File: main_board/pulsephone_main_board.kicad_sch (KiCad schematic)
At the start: 22 parts, among them J3 Conn_2Rows-35Pins_MountingPin, J4 Conn_2Rows-35Pins_MountingPin, J5 Conn_2Rows-35Pins_MountingPin, U1 XL1509-3.3, U2 PCM5102APWR, U4 TPS61202DRC

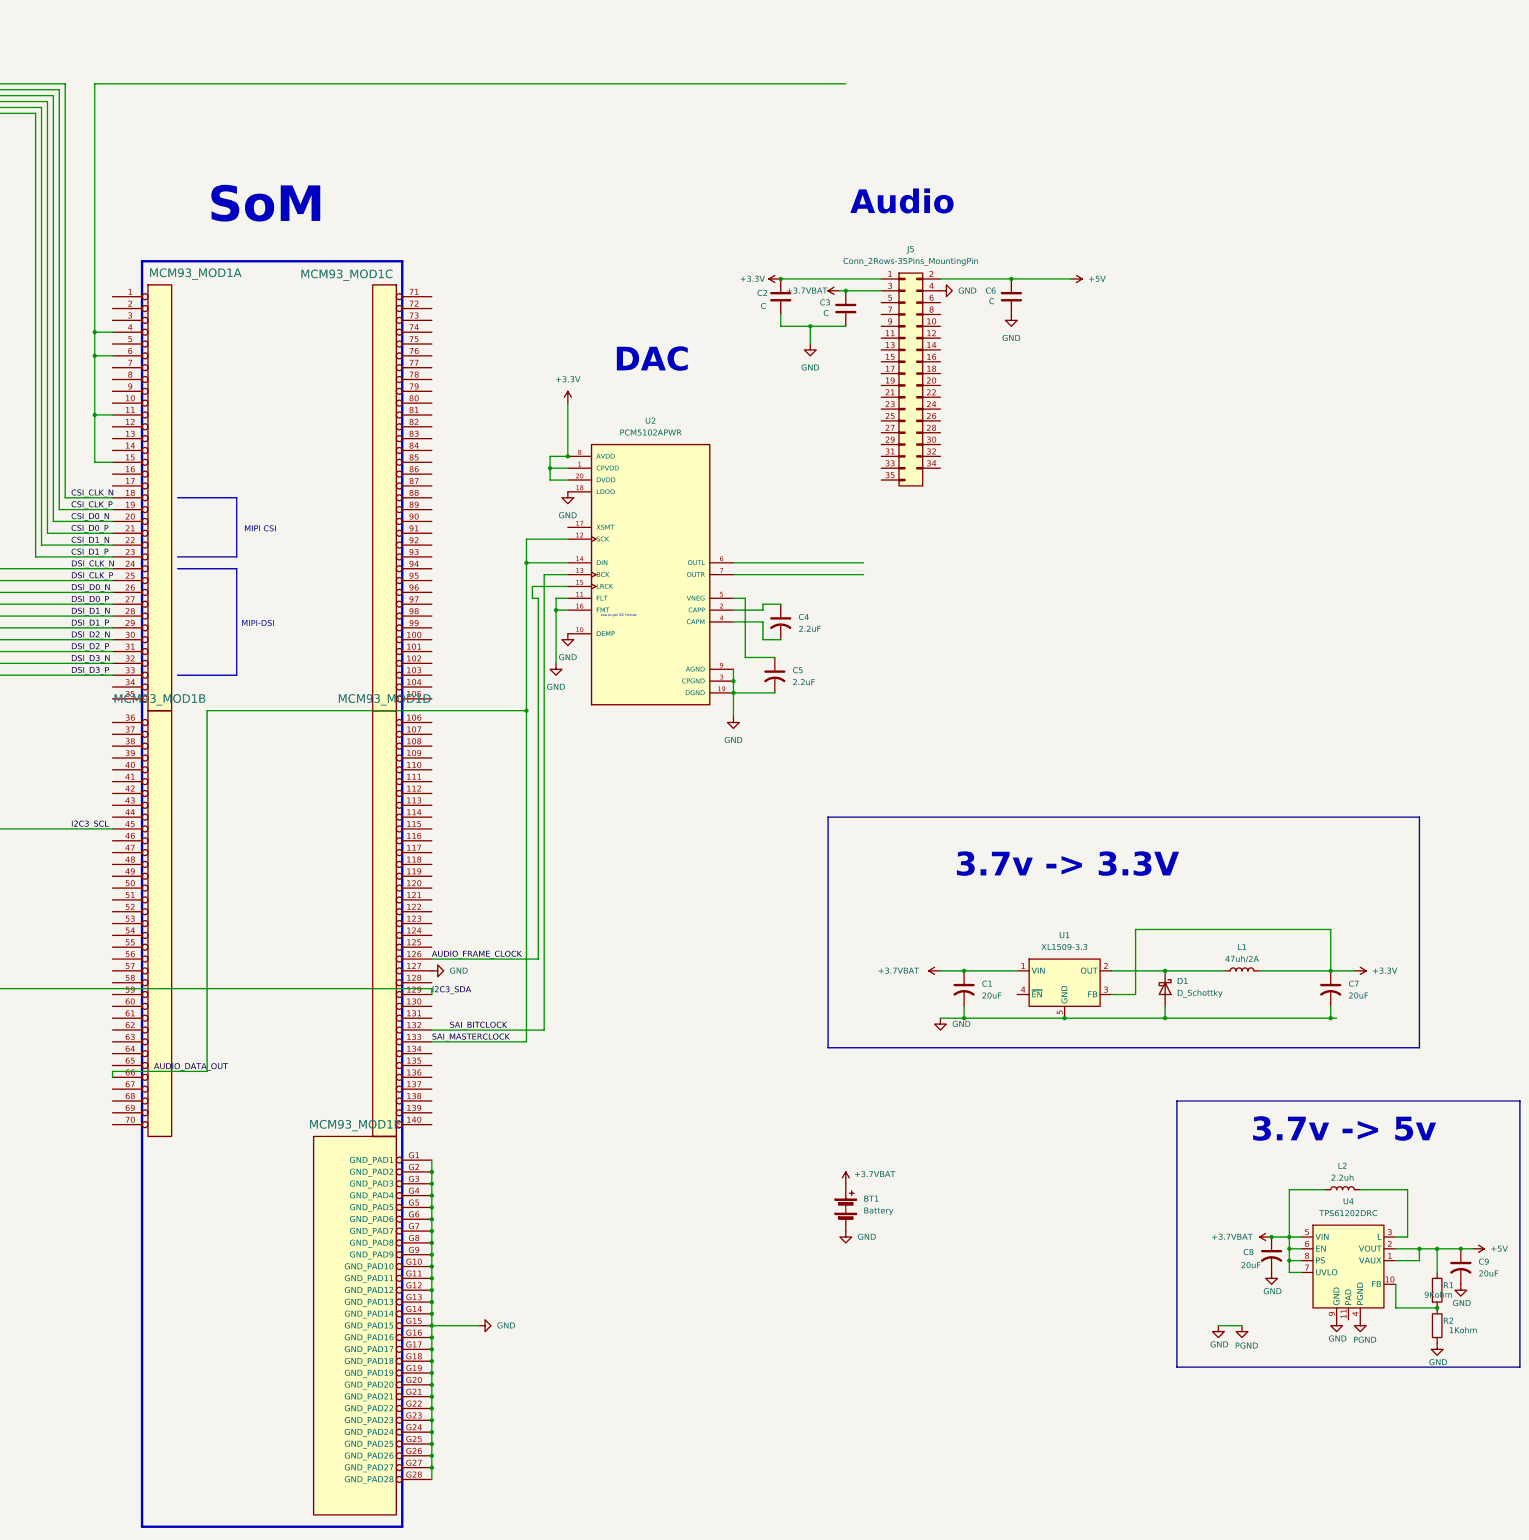
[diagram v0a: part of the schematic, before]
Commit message: Add in new, researched PMICs
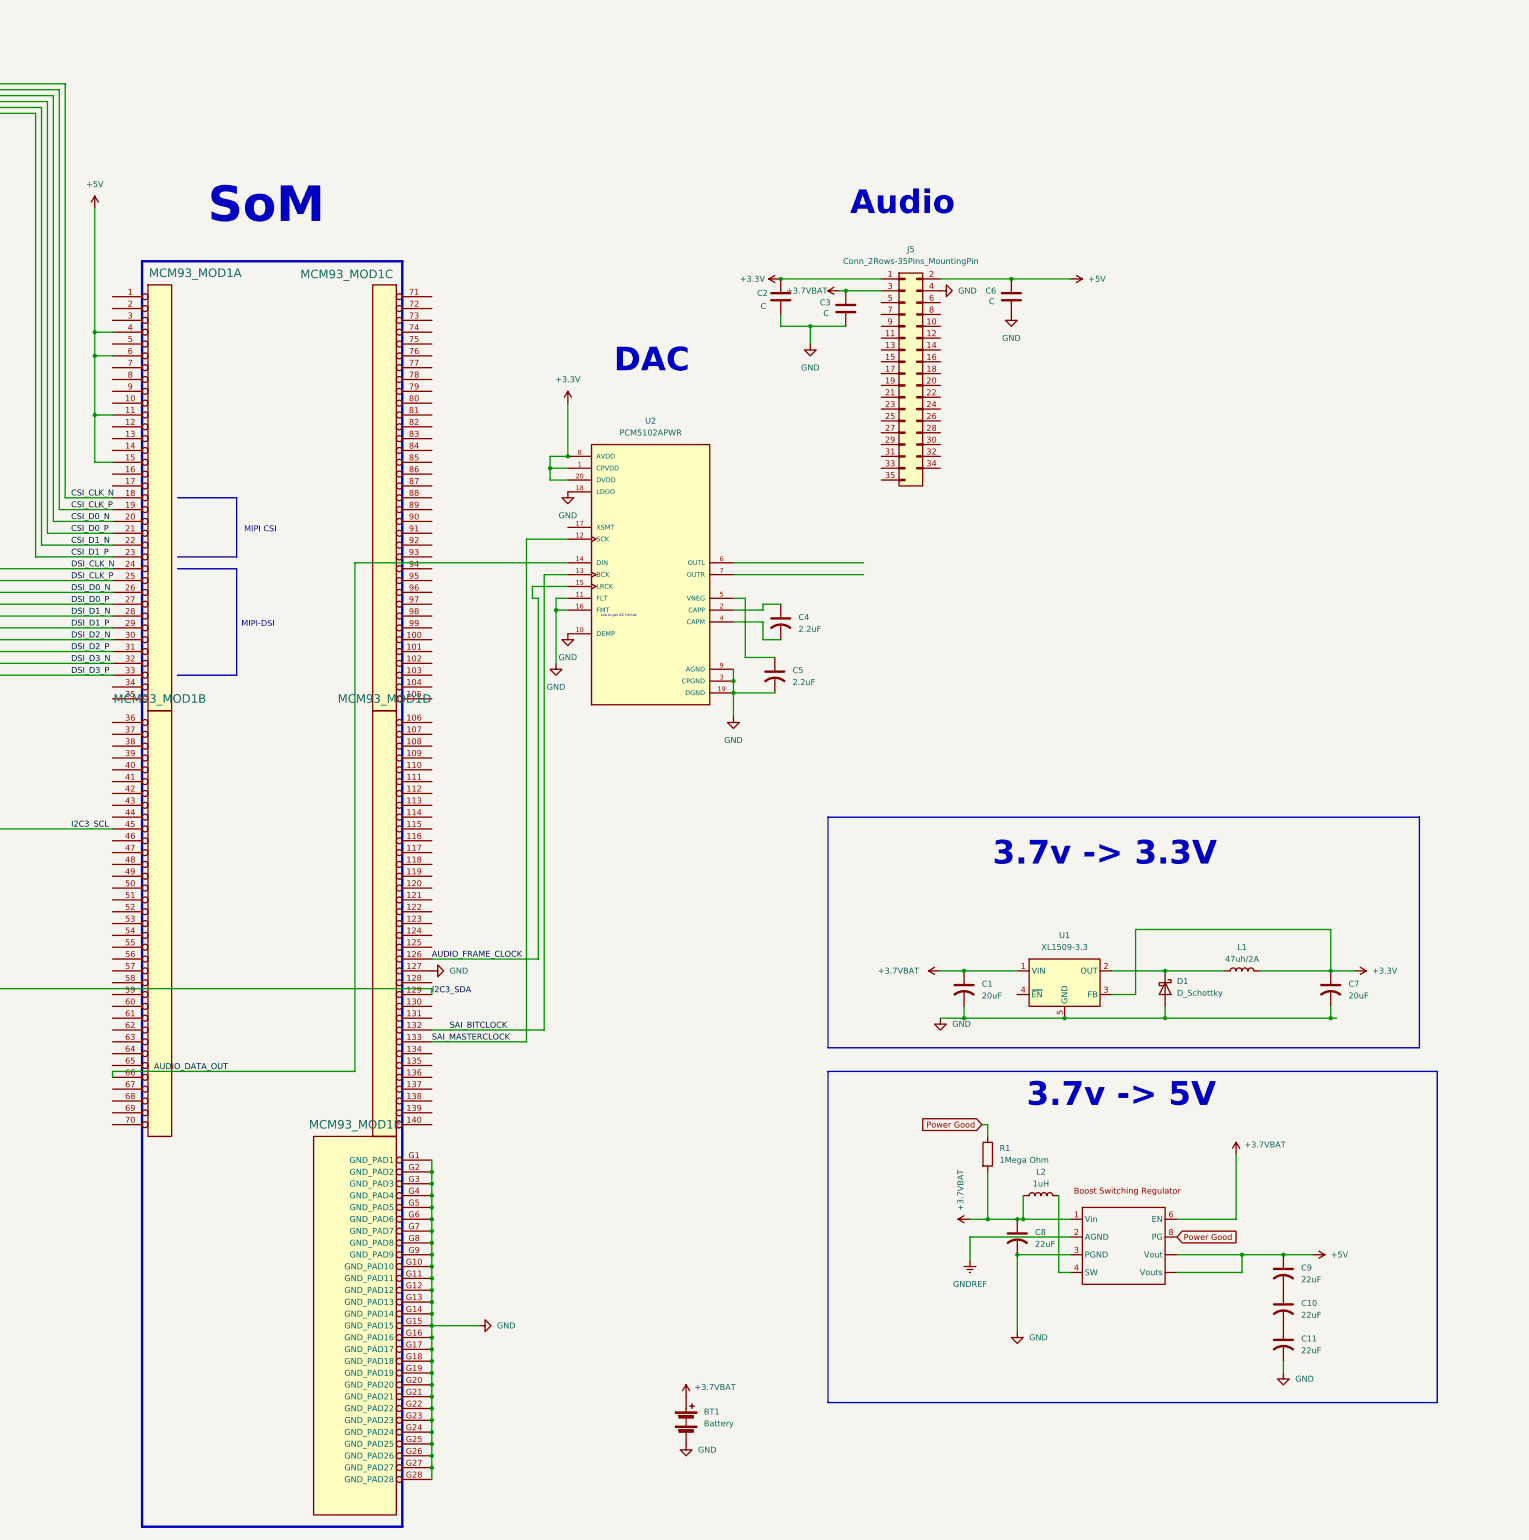
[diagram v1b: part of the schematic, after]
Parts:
- removed R2: 1Kohm, symbol Device:R
- removed U4: TPS61202DRC, Package_SON:Texas_S-PVSON-N10_ThermalVias, symbol Regulator_Switching:TPS61202DRC
- added C10, C11: 22uF, symbol Device:C_US
- added U3: ~, symbol New_Library:MIC2877-5.0YFT-TR
- C8, C9: value 20uF -> 22uF
- L2: value 2.2uh -> 1uH
- R1: value 9Kohm -> 1Mega Ohm
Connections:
- net +3.7VBAT: now also R1.2, U3.1 (Vin), U3.6 (EN)
- net +5V: now also MCM93_MOD1.11, MCM93_MOD1.15, MCM93_MOD1.4, MCM93_MOD1.6, U3. (Vouts); no longer R1.1
- net AUDIO_DATA_OUT: no longer MCM93_MOD1.133 (28), U2.12 (SCK)
- net GND: now also C11.2, U3.3 (PGND); no longer C9.2
- net at L2.2: now also U3.4 (SW)
- new net: C10.2, C11.1
- new net: C10.1, C9.2
- new net GNDREF: U3.2 (AGND)
- new net Power Good: R1.1, U3.8 (PG)
- new net SAI_MASTERCLOCK: MCM93_MOD1.133 (28), U2.12 (SCK)
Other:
- note added: "3.7v -> 5V"
- note removed: "3.7v -> 5v"
- moved on the sheet: BT1

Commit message: Work on completing schematics and starting pcb design
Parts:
- BT1: footprint (none) -> Connector_PinHeader_1.00mm:PinHeader_1x02_P1.00mm_Vertical_SMD_Pin1Left
- C1, C10, C11, C7, C8, C9: footprint (none) -> Capacitor_SMD:C_0603_1608Metric
- C2, C3, C6: value C -> 10uF; footprint (none) -> Capacitor_SMD:C_0603_1608Metric
- C4, C5: footprint Capacitor_SMD:C_0805_2012Metric -> Capacitor_SMD:C_0603_1608Metric
- D1: footprint (none) -> Diode_SMD:D_0201_0603Metric
- L1, L2: footprint (none) -> Inductor_SMD:L_0201_0603Metric
- R1: footprint (none) -> Resistor_SMD:R_0603_1608Metric_Pad0.98x0.95mm_HandSolder
- U3: footprint (none) -> MIC2877-5.0YFT-TR:VREG_MIC2877-AYFT-TR
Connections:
- net +3.7VBAT: now also U1.4 (~{EN})
- net at J5.8 (Pin_8): now also U2.6 (OUTL)
- net at J5.9 (Pin_9): now also U2.7 (OUTR)
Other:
- moved on the sheet: BT1, C1, C10, C11, C2, C3, C4, C5, C6, C7, C8, C9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

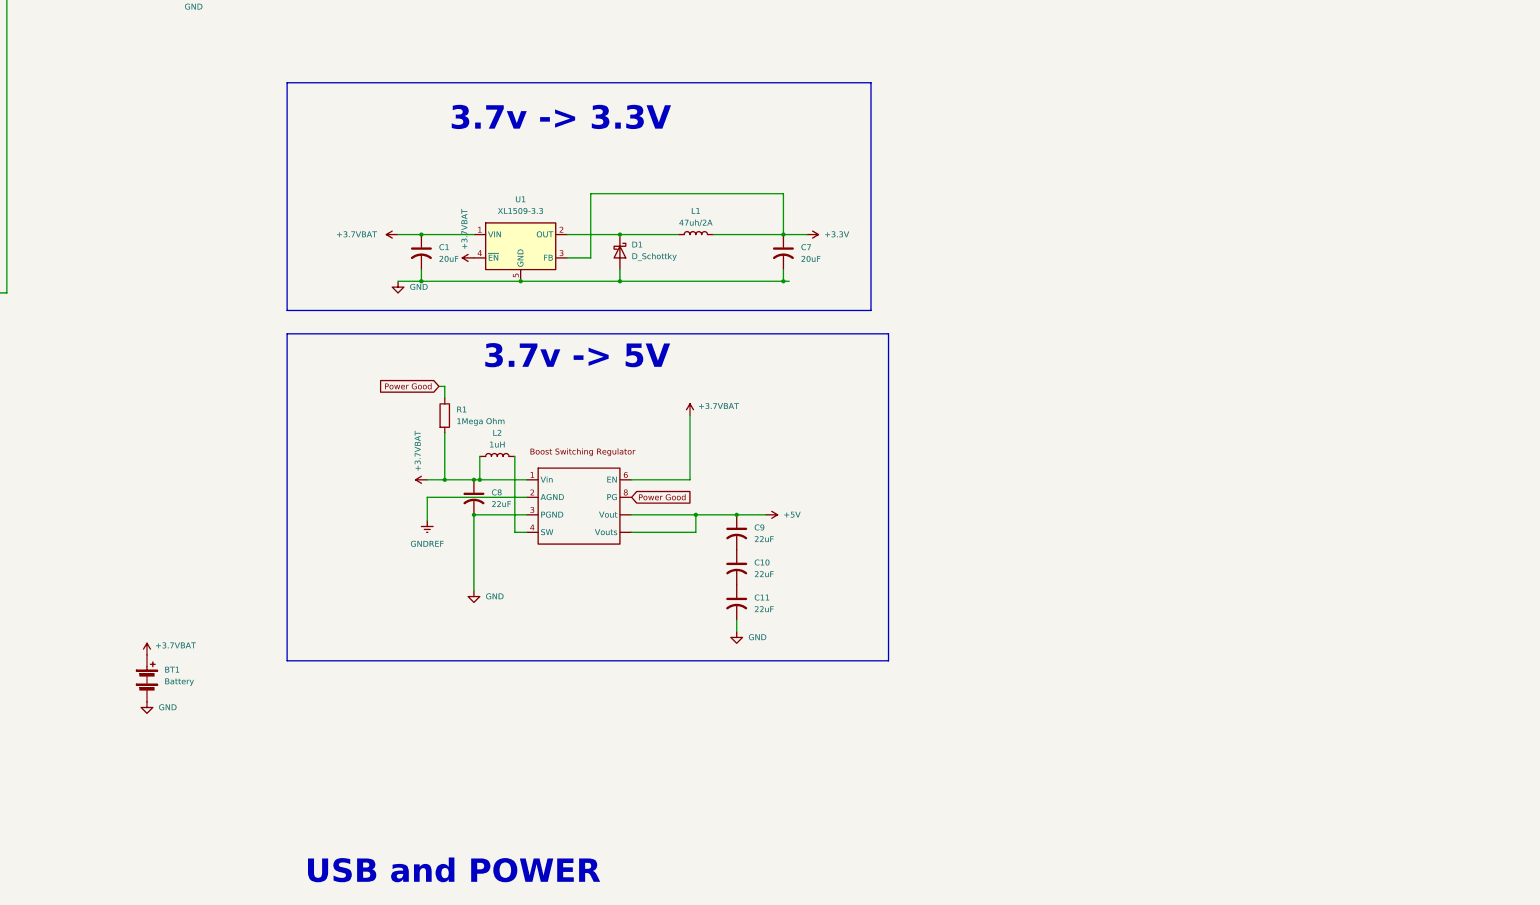
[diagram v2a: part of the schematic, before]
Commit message: Add charging IC and USB-C to schematic and PCB
Next step is to review PCB layout and start drawing traces
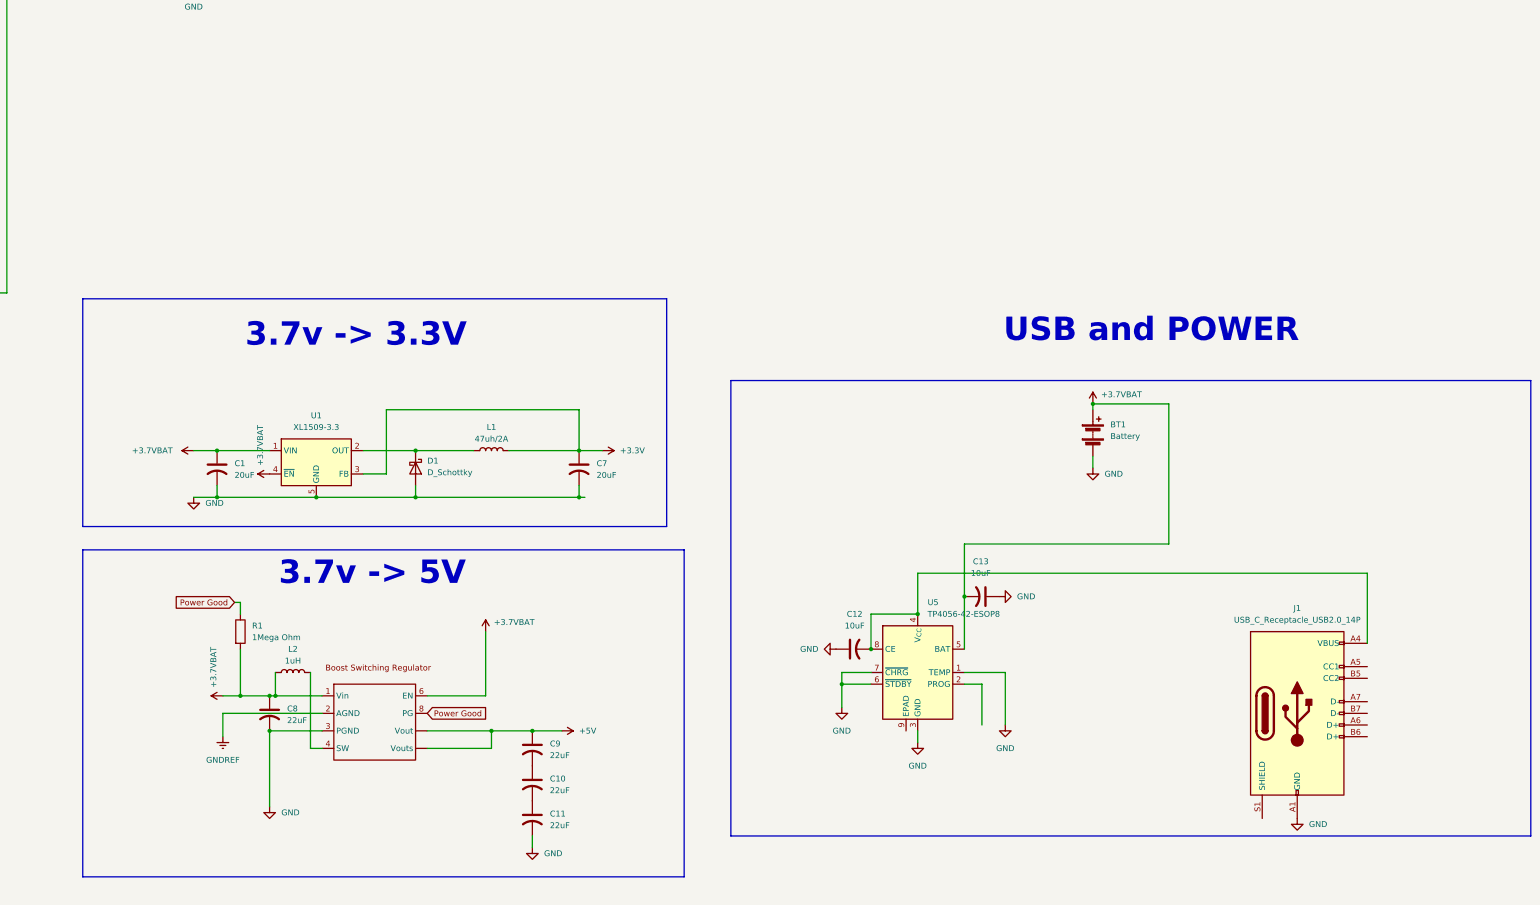
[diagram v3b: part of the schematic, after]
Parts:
- added C12, C13: 10uF, Capacitor_SMD:C_0603_1608Metric, symbol Device:C_US
- added J1: USB_C_Receptacle_USB2.0_14P, Connector_USB:USB_C_Receptacle_Amphenol_12401548E4-2A, symbol Connector:USB_C_Receptacle_USB2.0_14P
- added U5: TP4056-42-ESOP8, Package_SO:SOIC-8-1EP_3.9x4.9mm_P1.27mm_EP2.41x3.3mm_ThermalVias, symbol Battery_Management:TP4056-42-ESOP8
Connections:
- net +3.7VBAT: now also C13.2, U5.5 (BAT)
- net GND: now also C12.1, C13.1, J1.A1 (GND), J1.A12 (GND), J1.B1 (GND), J1.B12 (GND), U5.1 (TEMP), U5.3 (GND), U5.6 (~{STDBY}), U5.7 (~{CHRG})
- new net: C12.2, J1.A4 (VBUS), J1.A9 (VBUS), J1.B4 (VBUS), J1.B9 (VBUS), U5.4 (V_{CC}), U5.8 (CE)
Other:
- moved on the sheet: BT1, C1, C10, C11, C7, C8, C9, D1, L1, L2, R1, U1

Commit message: Redo PCB Routing, and added extra features
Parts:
- added C14, C15, C16, C17: 22uF, Capacitor_SMD:C_0603_1608Metric, symbol Device:C_US
- added D2: LED, LED_SMD:LED_0805_2012Metric, symbol Device:LED
- added H1, H2, H3, H4: MountingHole, MountingHole:MountingHole_3.2mm_M3, symbol Mechanical:MountingHole
- added R2, R3: 5.1 kΩ, Resistor_SMD:R_0805_2012Metric, symbol Device:R
- added SW1: SW_DPST_x2, Button_Switch_SMD:SW_Tactile_SPST_NO_Straight_CK_PTS636Sx25SMTRLFS, symbol Switch:SW_DPST_x2
- BT1: footprint Connector_PinHeader_1.00mm:PinHeader_1x02_P1.00mm_Vertical_SMD_Pin1Left -> Connector_PinHeader_1.00mm:PinHeader_1x02_P1.00mm_Horizontal
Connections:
- net GNDREF is gone; now on net GNDCHASSIS: U3.2 (AGND)
- net +3.7VBAT: now also D2.2 (A), SW1.2 (B); no longer BT1.1 (+), C1.1, U1.1 (VIN)
- net +5V: now also C1.1, U1.1 (VIN), C14.1, C15.1, C16.1, C17.1
- net GND: now also C14.2, C15.2, C16.2, C17.2, D2.1 (K), R2.2, R3.2
- net CAM_I2C_SCL: now reaches MCM93_MOD1.97 (27)
- net CAM_I2C_SCL: now also J3.11 (Pin_11)
- net CAM_I2C_SDA: now reaches MCM93_MOD1.98 (28)
- net CAM_I2C_SDA: now also J3.12 (Pin_12)
- net CAM_GPIO: now reaches MCM93_MOD1.131 (26)
- net CAM_GPIO: now also J3.13 (Pin_13)
- net USB_DN: now reaches MCM93_MOD1.139 (34)
- net USB_DN: now also J1.A7 (D-), J1.B7 (D-)
- net USB_DP: now reaches MCM93_MOD1.140 (35)
- net USB_DP: now also J1.A6 (D+), J1.B6 (D+)
- net RST: now reaches J4.17 (Pin_17)
- net RST: now also MCM93_MOD1.64 (29)
- net at J1.A5 (CC1): now also R2.1
- net at J1.B5 (CC2): now also R3.1
- net GNDCHASSIS: now reaches J1.S1 (SHIELD)
- new net: BT1.1 (+), SW1.1 (A)
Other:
- note added: "5v -> 3.3V"
- note added: "Main Board"
- note added: "Mounting"
- note removed: "3.7v -> 3.3V"
- moved on the sheet: BT1, C1, C10, C11, C12, C13, C2, C3, C4, C5, C6, C7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

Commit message: add extra ground pins to high speed MIPI LANES for reduction of signal coupling.
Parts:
- added J2: Conn_01x05, Connector_PinHeader_1.00mm:PinHeader_1x05_P1.00mm_Horizontal, symbol Connector_Generic:Conn_01x05
- added TP1, TP2, TP3, TP4: TestPoint, TestPoint:TestPoint_Pad_2.5x2.5mm, symbol Connector:TestPoint
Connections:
- net +3.3V: now also J3.13 (Pin_13), J4.23 (Pin_23), J2.1 (Pin_1), TP3.1; no longer J3.7 (Pin_7), J4.13 (Pin_13)
- net +3.7VBAT: now also J3.15 (Pin_15), J4.25 (Pin_25), TP4.1; no longer J3.9 (Pin_9), J4.15 (Pin_15)
- net +5V: now also J3.14 (Pin_14), J4.24 (Pin_24), J2.4 (Pin_4), TP2.1; no longer J3.8 (Pin_8), J4.14 (Pin_14)
- net CAM_GPIO: now also J3.19 (Pin_19); no longer J3.13 (Pin_13)
- net CAM_I2C_SCL: now also J3.17 (Pin_17); no longer J3.11 (Pin_11)
- net CAM_I2C_SDA: now also J3.18 (Pin_18); no longer J3.12 (Pin_12)
- net CSI_D0_N: now also J3.5 (Pin_5); no longer J3.3 (Pin_3)
- net CSI_D0_P: now also J3.6 (Pin_6); no longer J3.4 (Pin_4)
- net CSI_D1_N: now also J3.9 (Pin_9); no longer J3.5 (Pin_5)
- net CSI_D1_P: now also J3.10 (Pin_10); no longer J3.6 (Pin_6)
- net DSI_D0_N: now also J4.5 (Pin_5); no longer J4.3 (Pin_3)
- net DSI_D0_P: now also J4.6 (Pin_6); no longer J4.4 (Pin_4)
- net DSI_D1_N: now also J4.9 (Pin_9); no longer J4.5 (Pin_5)
- net DSI_D1_P: now also J4.10 (Pin_10); no longer J4.6 (Pin_6)
- net DSI_D2_N: now also J4.13 (Pin_13); no longer J4.7 (Pin_7)
- net DSI_D2_P: now also J4.14 (Pin_14); no longer J4.8 (Pin_8)
- net DSI_D3_N: now also J4.17 (Pin_17); no longer J4.9 (Pin_9)
- net DSI_D3_P: now also J4.18 (Pin_18); no longer J4.10 (Pin_10)
- net GND: now also J3.11 (Pin_11), J3.12 (Pin_12), J3.16 (Pin_16), J3.3 (Pin_3), J3.4 (Pin_4), J3.7 (Pin_7), J3.8 (Pin_8), J4.11 (Pin_11), J4.12 (Pin_12), J4.15 (Pin_15), J4.19 (Pin_19), J4.20 (Pin_20), J4.26 (Pin_26), J4.3 (Pin_3), J4.4 (Pin_4), J4.7 (Pin_7), J4.8 (Pin_8), J2.5 (Pin_5), TP1.1; no longer J3.10 (Pin_10)
- net I2C3_SCL: now also J4.21 (Pin_21); no longer J4.11 (Pin_11)
- net I2C3_SDA: now also J4.22 (Pin_22); no longer J4.12 (Pin_12)
- net RST: now also J4.27 (Pin_27), MCM93_MOD1.108 (3); no longer J4.17 (Pin_17), MCM93_MOD1.64 (29)
- net UART_TX: now reaches MCM93_MOD1.63 (28)
- net UART_TX: now also J2.3 (Pin_3)
- new net UART_RX: J2.2 (Pin_2), MCM93_MOD1.64 (29)
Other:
- note added: "EXPOSED UART"
- note added: "Test Points"
